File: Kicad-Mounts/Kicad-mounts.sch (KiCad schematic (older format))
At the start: 12 parts, among them P1 CONN_10, P2 CONN_10, P3 CONN_6X2, P4 CONN_3, P5 CONN_3, P6 CONN_3, U2 TPS77033

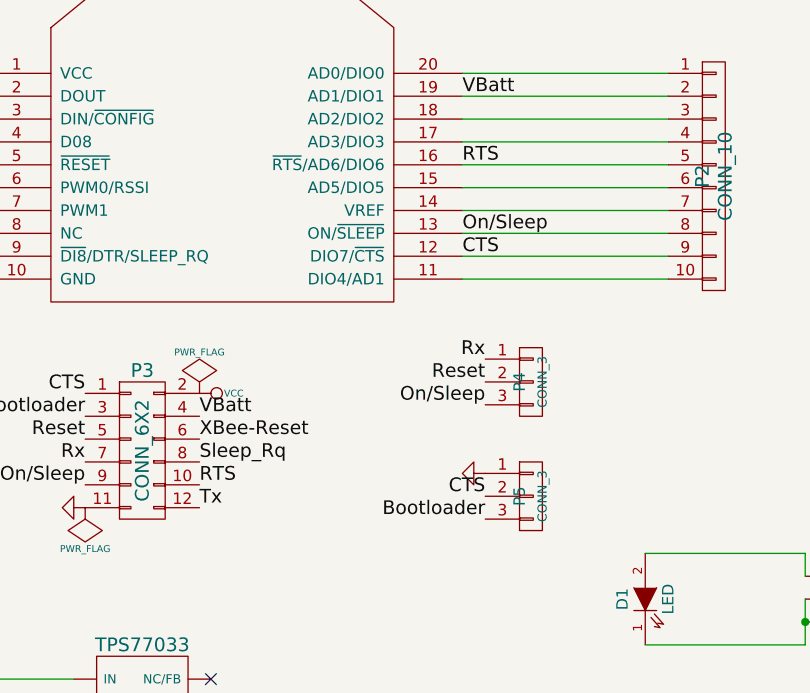
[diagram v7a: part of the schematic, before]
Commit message: Change RTS pin to Association pin for possible monitoring. Update README
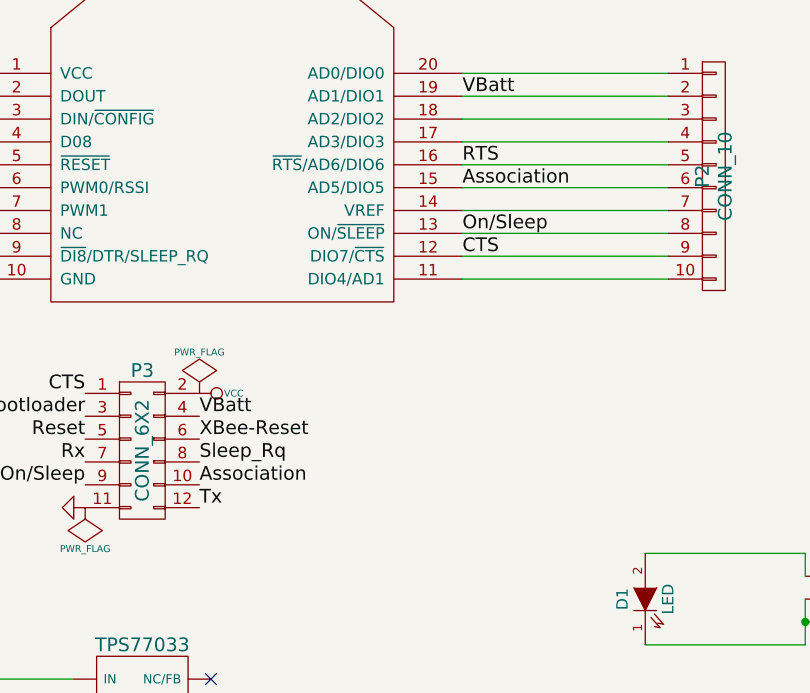
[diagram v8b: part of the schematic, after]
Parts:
- removed P4, P5: CONN_3, Photodiode:pin_header_2mm_1x3, symbol CONN_01X03
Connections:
- net RTS: no longer P3.10 (P10)
- net Association: now reaches P2.6 (P6), XB1.15 (AD5/DIO5)
- net Association: now also P3.10 (P10)
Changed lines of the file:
@@
-$EndComp
-$Comp
-L CONN_01X03 P4
-U 1 1 53F674B3
-P 5400 4750
-F 0 "P4" V 5350 4750 50  0000 C CNN
-F 1 "CONN_3" V 5450 4750 40  0000 C CNN
-F 2 "Photodiode:pin_header_2mm_1x3" H 5400 4750 60  0001 C CNN
-F 3 "" H 5400 4750 60  0000 C CNN
-	1    5400 4750
-	1    0    0    -1
-$EndComp
-$Comp
-L CONN_01X03 P5
-U 1 1 53F6753C
-P 5400 5250
-F 0 "P5" V 5350 5250 50  0000 C CNN
-F 1 "CONN_3" V 5450 5250 40  0000 C CNN
-F 2 "Photodiode:pin_header_2mm_1x3" H 5400 5250 60  0001 C CNN
-F 3 "" H 5400 5250 60  0000 C CNN
-	1    5400 5250
-	1    0    0    -1
 $EndComp
 $Comp
@@
 	0    1    1    0
 $EndComp
-Text Label 5200 4650 2    60   ~ 0
-Rx
-Text Label 5200 4750 2    60   ~ 0
-Reset
-Text Label 5200 4850 2    60   ~ 0
-On/Sleep
-Text Label 5200 5350 2    60   ~ 0
-Bootloader
 Text Label 3000 3800 2    60   ~ 0
 XBee-Reset
@@
 $EndComp
 Text Label 3950 5200 0    60   ~ 0
-RTS
-$Comp
-L GND #PWR06
-U 1 1 53FEF8A0
-P 5200 5150
-F 0 "#PWR06" H 5200 5150 30  0001 C CNN
-F 1 "GND" H 5200 5080 30  0001 C CNN
-F 2 "" H 5200 5150 60  0000 C CNN
-F 3 "" H 5200 5150 60  0000 C CNN
-	1    5200 5150
-	0    1    1    0
-$EndComp
+Association
 $Comp
 L TPS77033 U2
@@
 Connection ~ 4600 6200
 Connection ~ 2800 6050
-Text Label 5200 5250 2    60   ~ 0
-CTS
+Text Label 5100 3900 0    60   ~ 0
+Association
 $EndSCHEMATC
